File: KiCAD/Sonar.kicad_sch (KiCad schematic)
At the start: 0 parts

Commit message: Finished routing
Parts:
- added H1, H2, H3, H4: MountingHole, MountingHole:MountingHole_3.5mm_Pad_Via, symbol Connectors:MountingHole
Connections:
- new net GND: H1.1, H2.1, H3.1, H4.1

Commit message: Added RRSG and RadarMasters logos
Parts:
- added H5: RRSG, Logos:RRSG, symbol Logos:RRSG
- added H6: RadarMasters, Logos:RadarMasters, symbol Logos:RadarMasters
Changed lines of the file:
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@@
+		)
+	)
+	(symbol
+		(lib_id "Logos:RRSG")
+		(at 106.68 165.1 0)
+		(unit 1)
+		(body_style 1)
+		(exclude_from_sim no)
+		(in_bom no)
+		(on_board yes)
+		(in_pos_files yes)
+		(dnp no)
+		(property "Reference" "H5"
+			(at 101.6 161.29 0)
+			(show_name no)
+			(do_not_autoplace no)
+			(effects
+				(font
+					(size 1.27 1.27)
+				)
+				(justify left)
+			)
+		)
+		(property "Value" "RRSG"
+			(at 121.285 164.465 0)
+			(hide yes)
+			(show_name no)
+			(do_not_autoplace no)
+			(effects
+				(font
+					(size 1.27 1.27)
+				)
+				(justify left)
+			)
+		)
+		(property "Footprint" "Logos:RRSG"
+			(at 121.285 167.005 0)
+			(hide yes)
+			(show_name no)
+			(do_not_autoplace no)
+			(effects
+				(font
+					(size 1.27 1.27)
+				)
+				(justify left)
+			)
+		)
+		(property "Datasheet" ""
+			(at 111.76 165.1 0)
+			(hide yes)
+			(show_name no)
+			(do_not_autoplace no)
+			(effects
+				(font
+					(size 1.27 1.27)
+				)
+				(justify left)
+			)
+		)
+		(property "Description" "RRSG Logo"
+			(at 126.746 169.418 0)
+			(hide yes)
+			(show_name no)
+			(do_not_autoplace no)
+			(effects
+				(font
+					(size 1.27 1.27)
+				)
+			)
+		)
+		(property "BOM" "No"
+			(at 121.285 161.925 0)
+			(hide yes)
+			(show_name no)
+			(do_not_autoplace no)
+			(effects
+				(font
+					(size 1.27 1.27)
+				)
+				(justify left)
+			)
+		)
+		(instances
+			(project "Sonar"
+				(path "/28f9d169-72cd-4bf2-894c-12741d733c98"
+					(reference "H5")
+					(unit 1)
+				)
+			)
+		)
+	)
+	(symbol
+		(lib_id "Logos:RadarMasters")
+		(at 106.68 175.26 0)
+		(unit 1)
+		(body_style 1)
+		(exclude_from_sim no)
+		(in_bom no)
+		(on_board yes)
+		(in_pos_files yes)
+		(dnp no)
+		(property "Reference" "H6"
+			(at 101.6 171.45 0)
+			(show_name no)
+			(do_not_autoplace no)
+			(effects
+				(font
+					(size 1.27 1.27)
+				)
+				(justify left)
+			)
+		)
+		(property "Value" "RadarMasters"
+			(at 121.285 174.625 0)
+			(hide yes)
+			(show_name no)
+			(do_not_autoplace no)
+			(effects
+				(font
+					(size 1.27 1.27)
+				)
+				(justify left)
+			)
+		)
+		(property "Footprint" "Logos:RadarMasters"
+			(at 121.285 177.165 0)
+			(hide yes)
+			(show_name no)
+			(do_not_autoplace no)
+			(effects
+				(font
+					(size 1.27 1.27)
+				)
+				(justify left)
+			)
+		)
+		(property "Datasheet" ""
+			(at 111.76 175.26 0)
+			(hide yes)
+			(show_name no)
+			(do_not_autoplace no)
+			(effects
+				(font
+					(size 1.27 1.27)
+				)
+				(justify left)
+			)
+		)
+		(property "Description" "RadarMasters Logo"
+			(at 126.746 179.578 0)
+			(hide yes)
+			(show_name no)
+			(do_not_autoplace no)
+			(effects
+				(font
+					(size 1.27 1.27)
+				)
+			)
+		)
+		(property "BOM" "No"
+			(at 121.285 172.085 0)
+			(hide yes)
+			(show_name no)
+			(do_not_autoplace no)
+			(effects
+				(font
+					(size 1.27 1.27)
+				)
+				(justify left)
+			)
+		)
+		(instances
+			(project "Sonar"
+				(path "/28f9d169-72cd-4bf2-894c-12741d733c98"
+					(reference "H6")
+					(unit 1)
+				)
+			)
 		)
 	)

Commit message: Cosmetics and fiducials
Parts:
- added F1, F2, F3, F4: (no value), Fiducial:Fiducial_1mm_Mask3mm, symbol Mechanical:Fiducial

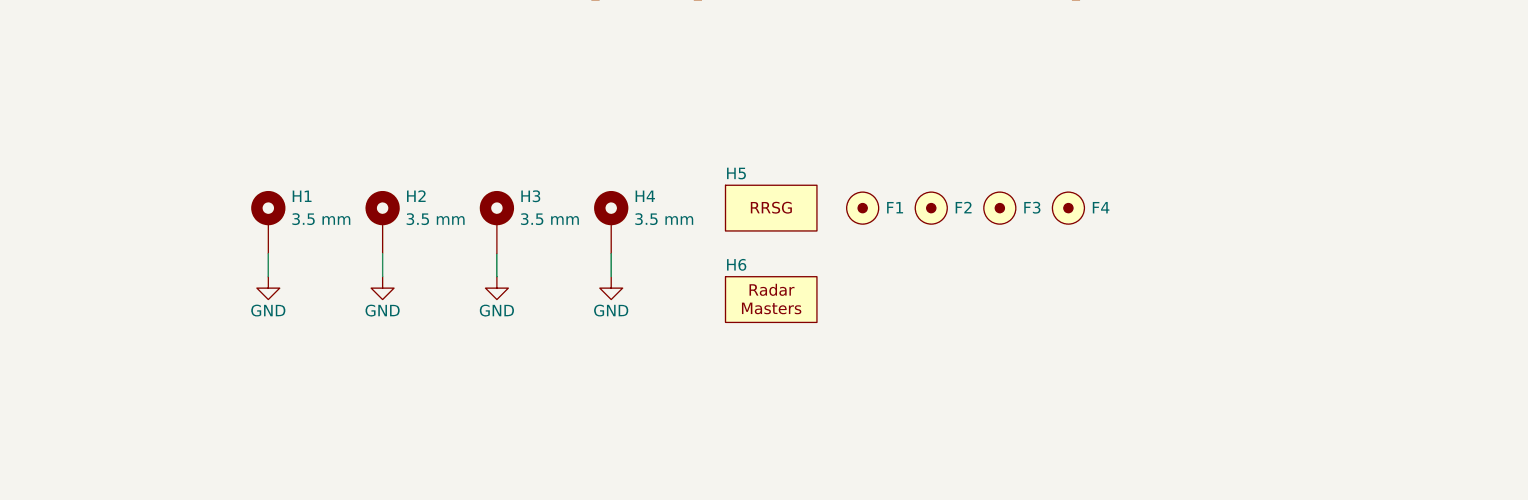
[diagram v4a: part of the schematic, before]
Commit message: Added test-points
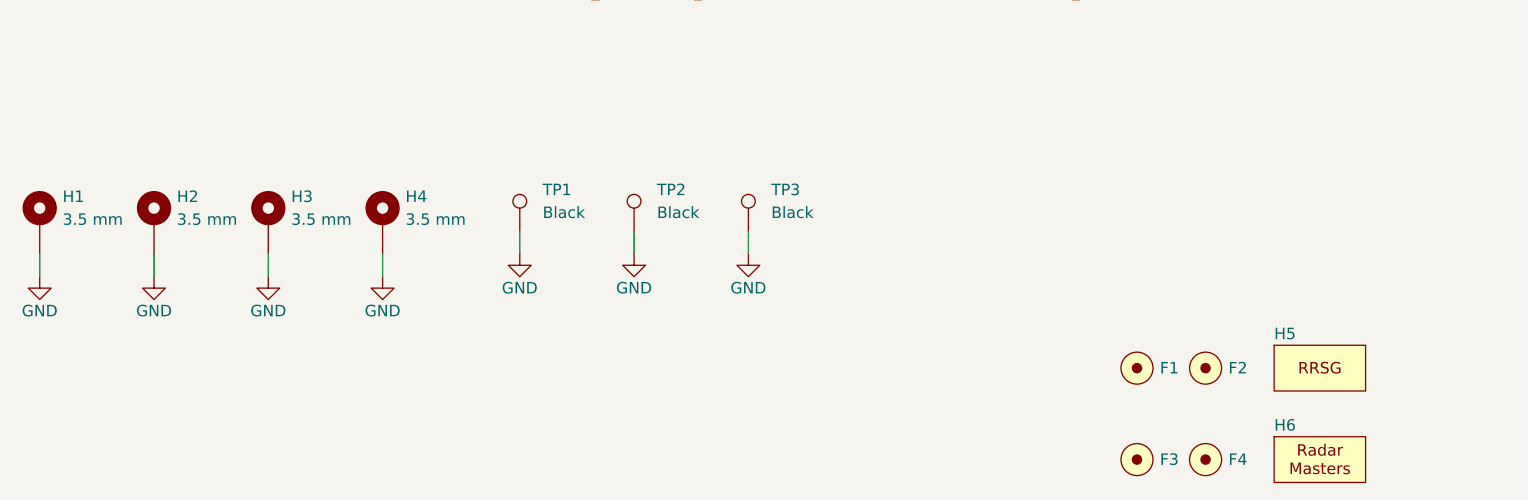
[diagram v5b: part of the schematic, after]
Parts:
- added TP1, TP2, TP3: Keystone_5011_Black, TestPoint:TestPoint_Keystone_5010-5014_Multipurpose, symbol Connectors:Keystone_5011_Black
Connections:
- net GND: now also TP1.1, TP2.1, TP3.1
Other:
- moved on the sheet: F1, F2, F3, F4, H1, H2, H3, H4, H5, H6

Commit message: Set up and exported the BOM
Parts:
- H1, H2, H3, H4: now left out of the parts list
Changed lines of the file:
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@@
+			)
+		)
+		(property "ManPartNo" ""
+			(at 154.94 190.5 0)
+			(hide yes)
+			(show_name no)
+			(do_not_autoplace no)
+			(effects
+				(font
+					(size 1.27 1.27)
+				)
 			)
 		)
@@
 		(body_style 1)
 		(exclude_from_sim no)
-		(in_bom yes)
+		(in_bom no)
 		(on_board yes)
 		(in_pos_files yes)
@@
 				)
 				(justify left)
+			)
+		)
+		(property "ManPartNo" ""
+			(at 50.8 165.1 0)
+			(hide yes)
+			(show_name no)
+			(do_not_autoplace no)
+			(effects
+				(font
+					(size 1.27 1.27)
+				)
 			)
 		)
@@
 		(body_style 1)
 		(exclude_from_sim no)
-		(in_bom yes)
+		(in_bom no)
 		(on_board yes)
 		(in_pos_files yes)
@@
 				)
 				(justify left)
+			)
+		)
+		(property "ManPartNo" ""
+			(at 25.4 165.1 0)
+			(hide yes)
+			(show_name no)
+			(do_not_autoplace no)
+			(effects
+				(font
+					(size 1.27 1.27)
+				)
 			)
 		)
@@
 			)
 		)
+		(property "ManPartNo" ""
+			(at 147.32 180.34 0)
+			(hide yes)
+			(show_name no)
+			(do_not_autoplace no)
+			(effects
+				(font
+					(size 1.27 1.27)
+				)
+			)
+		)
 		(instances
 			(project "Sonar"
@@
 			)
 		)
+		(property "ManPartNo" ""
+			(at 104.14 167.64 0)
+			(hide yes)
+			(show_name no)
+			(do_not_autoplace no)
+			(effects
+				(font
+					(size 1.27 1.27)
+				)
+			)
+		)
 		(pin "1"
 		)
@@
 			)
 		)
+		(property "ManPartNo" ""
+			(at 78.74 167.64 0)
+			(hide yes)
+			(show_name no)
+			(do_not_autoplace no)
+			(effects
+				(font
+					(size 1.27 1.27)
+				)
+			)
+		)
 		(pin "1"
 		)
@@
 			)
 		)
+		(property "ManPartNo" ""
+			(at 154.94 180.34 0)
+			(hide yes)
+			(show_name no)
+			(do_not_autoplace no)
+			(effects
+				(font
+					(size 1.27 1.27)
+				)
+			)
+		)
 		(instances
 			(project "Sonar"
@@
 			)
 		)
+		(property "ManPartNo" ""
+			(at 147.32 190.5 0)
+			(hide yes)
+			(show_name no)
+			(do_not_autoplace no)
+			(effects
+				(font
+					(size 1.27 1.27)
+				)
+			)
+		)
 		(instances
 			(project "Sonar"
@@
 		(body_style 1)
 		(exclude_from_sim no)
-		(in_bom yes)
+		(in_bom no)
 		(on_board yes)
 		(in_pos_files yes)
@@
 				)
 				(justify left)
+			)
+		)
+		(property "ManPartNo" ""
+			(at 38.1 165.1 0)
+			(hide yes)
+			(show_name no)
+			(do_not_autoplace no)
+			(effects
+				(font
+					(size 1.27 1.27)
+				)
 			)
 		)
@@
 		(body_style 1)
 		(exclude_from_sim no)
-		(in_bom yes)
+		(in_bom no)
 		(on_board yes)
 		(in_pos_files yes)
@@
 				)
 				(justify left)
+			)
+		)
+		(property "ManPartNo" ""
+			(at 63.5 165.1 0)
+			(hide yes)
+			(show_name no)
+			(do_not_autoplace no)
+			(effects
+				(font
+					(size 1.27 1.27)
+				)
 			)
 		)
@@
 			)
 		)
+		(property "ManPartNo" ""
+			(at 91.44 167.64 0)
+			(hide yes)
+			(show_name no)
+			(do_not_autoplace no)
+			(effects
+				(font
+					(size 1.27 1.27)
+				)
+			)
+		)
 		(pin "1"
 		)
@@
 			)
 		)
+		(property "ManPartNo" ""
+			(at 167.64 182.88 0)
+			(hide yes)
+			(show_name no)
+			(do_not_autoplace no)
+			(effects
+				(font
+					(size 1.27 1.27)
+				)
+			)
+		)
 		(instances
 			(project "Sonar"
@@
 			)
 		)
+		(property "ManPartNo" ""
+			(at 167.64 193.04 0)
+			(hide yes)
+			(show_name no)
+			(do_not_autoplace no)
+			(effects
+				(font
+					(size 1.27 1.27)
+				)
+			)
+		)

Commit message: Added title block and version text
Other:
- company: (none) -> University of Cape Town
- title: (none) -> Sonar Top Level
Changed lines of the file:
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@@
 	(generator_version "10.0")
 	(paper "A4")
+	(title_block
+		(title "Sonar Top Level")
+		(date "2026-05-09")
+		(rev "v1.0")
+		(company "University of Cape Town")
+	)
 	(wire
 		(pts
@@
 			(project "Sonar"
 				(path "/28f9d169-72cd-4bf2-894c-12741d733c98"
-					(page "7")
+					(page "4")
 				)
 			)
@@
 			(project "Sonar"
 				(path "/28f9d169-72cd-4bf2-894c-12741d733c98"
-					(page "6")
+					(page "3")
 				)
 			)
@@
 			(project "Sonar"
 				(path "/28f9d169-72cd-4bf2-894c-12741d733c98"
-					(page "3")
+					(page "5")
 				)
 			)
